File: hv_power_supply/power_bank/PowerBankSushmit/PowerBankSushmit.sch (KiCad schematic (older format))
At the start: 48 parts, among them J1 CONN_01x02, J2 CONN_01x02, J3 USB_A, Q1 SSM3K333R, U1 USB_MicroB, U2 MCP73871T-2CCI_ML-formula, U3 TPS61090RSAR-formula

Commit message: Edited paths and references to match the team
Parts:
- removed C1, C2, C3, C4: C_10uF, footprints:C_0805_OEM, symbol formula:C_10uF-formula
- removed C5: C_10nF, footprints:C_0805_OEM, symbol formula:C_10nF-formula
- removed C6: C_2.2uF, footprints:C_0805_OEM, symbol formula:C_10uF-formula
- removed C7: C_100uF, footprints:C_0805_OEM, symbol formula:C_10uF-formula
- removed D1, D3, D4: LED_0805, footprints:LED_0805_OEM, symbol formula:LED_0805-formula
- removed D2: LED_0805_Amber, footprints:LED_0805_OEM, symbol formula:LED_0805_Amber-formula
- removed F1: 1.5A_Fuse, footprints:Fuse_1206, symbol formula:1.5A_Fuse-formula
- removed J1, J2: CONN_01x02, Connector_PinHeader_2.54mm:PinHeader_1x02_P2.54mm_Vertical, symbol formula:CONN_01x02-formula
- removed L1: L_6.8uH, symbol formula:L_6.8uH-formula
- removed Q1: SSM3K333R, footprints:SOT-23F, symbol formula:SSM3K333R-formula
- removed R1: R_75K, footprints:R_0805_OEM, symbol formula:formula_R_1K
- removed R10, R8: R_100K, footprints:R_0805_OEM, symbol formula:formula_R_1K
- removed R11, R5: R_1.87M, footprints:R_0805_OEM, symbol formula:formula_R_1K
- removed R12, R9: R_200K, footprints:R_0805_OEM, symbol formula:formula_R_1K
- removed R13, R17: R_1k, footprints:R_0805_OEM, symbol formula:formula_R_1K
- removed R14, R16, R18: R_1K, footprints:R_0805_OEM, symbol formula:formula_R_1K
- removed R15: R_10K, footprints:R_0805_OEM, symbol formula:formula_R_1K
- removed R2, R4: R_49.9K, footprints:R_0805_OEM, symbol formula:formula_R_1K
- removed R3: R_43K, footprints:R_0805_OEM, symbol formula:formula_R_1K
- removed R6: R_340K, footprints:R_0805_OEM, symbol formula:formula_R_1K
- removed R7: R_270K, footprints:R_0805_OEM, symbol formula:formula_R_1K
- removed TP1, TP2, TP3, TP4, TP5: TP, footprints:tp_1.6mm, symbol formula:TP-formula
- removed U1: USB_MicroB, Connectors_USB:USB_Micro-B_Molex-105017-0001, symbol formula:USB_MicroB-formula
- removed U2: MCP73871T-2CCI_ML-formula, footprints:MCP73871T, symbol formula:MCP73871T-2CCI_ML-formula
- removed U3: TPS61090RSAR-formula, footprints:TPS61090RSAR, symbol formula:TPS61090RSAR-formula
- added C1, C2, C3, C4: C_10uF, footprints:C_0805_OEM, symbol formula:C_10uF
- added C5: C_10nF, footprints:C_0805_OEM, symbol formula:C_10nF
- added C6: C_2.2uF, footprints:C_0805_OEM, symbol formula:C_2.2uF
- added C7: C_100uF, footprints:C_1812_OEM, symbol formula:C_100uF
- added D1, D3, D4: LED_0805, footprints:LED_0805_OEM, symbol formula:LED_0805
- added D2: LED_0805_Amber, footprints:LED_0805_OEM, symbol formula:LED_0805_Amber
- added F1: 1.5A_Fuse, footprints:Fuse_1206, symbol formula:1.5A_Fuse
- added J1, J2: CONN_01x02, Connector_PinHeader_2.54mm:PinHeader_1x02_P2.54mm_Vertical, symbol formula:CONN_01x02
- added L1: L_6.8uH, symbol formula:L_6.8uH
- added Q1: SSM3K333R, footprints:SOT-23F, symbol formula:SSM3K333R
- added R1: R_75k, footprints:R_0805_OEM, symbol formula:R_75k
- added R10, R8: R_100K, footprints:R_0805_OEM, symbol formula:R_100K
- added R11, R5: R_1.87M, footprints:R_0805_OEM, symbol formula:R_1.87M
- added R12, R9: R_200K, footprints:R_0805_OEM, symbol formula:R_200K
- added R13, R14, R16, R17, R18: R_1K, footprints:R_0805_OEM, symbol formula:R_1K
- added R15: R_10K, footprints:R_0805_OEM, symbol formula:R_10K
- added R2, R4: R_49.9K, footprints:R_0805_OEM, symbol formula:R_49.9K
- added R3: R_43k, footprints:R_0805_OEM, symbol formula:R_43k
- added R6: R_340K, footprints:R_0805_OEM, symbol formula:R_340K
- added R7: R_270K, footprints:R_0805_OEM, symbol formula:R_270K
- added TP1, TP2, TP3, TP4, TP5: TP, footprints:tp_1.6mm, symbol formula:TP
- added U1: USB_MicroB, Connectors_USB:USB_Micro-B_Molex-105017-0001, symbol formula:USB_MicroB
- added U2: MCP73871T-2CCI_ML, footprints:MCP73871T, symbol formula:MCP73871T-2CCI_ML
- added U3: TPS61090RSAR, footprints:TPS61090RSAR, symbol formula:TPS61090RSAR
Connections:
- net labels added: GNDPWR, VBATT
- net labels removed: GNDPWR-formula, VBATT-formula
- wire segments 111 -> 109
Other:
- note added: "Resistor values are specific to IOS"
- note removed: "Resistor valyes are specific to IOS"
- moved on the sheet: J3

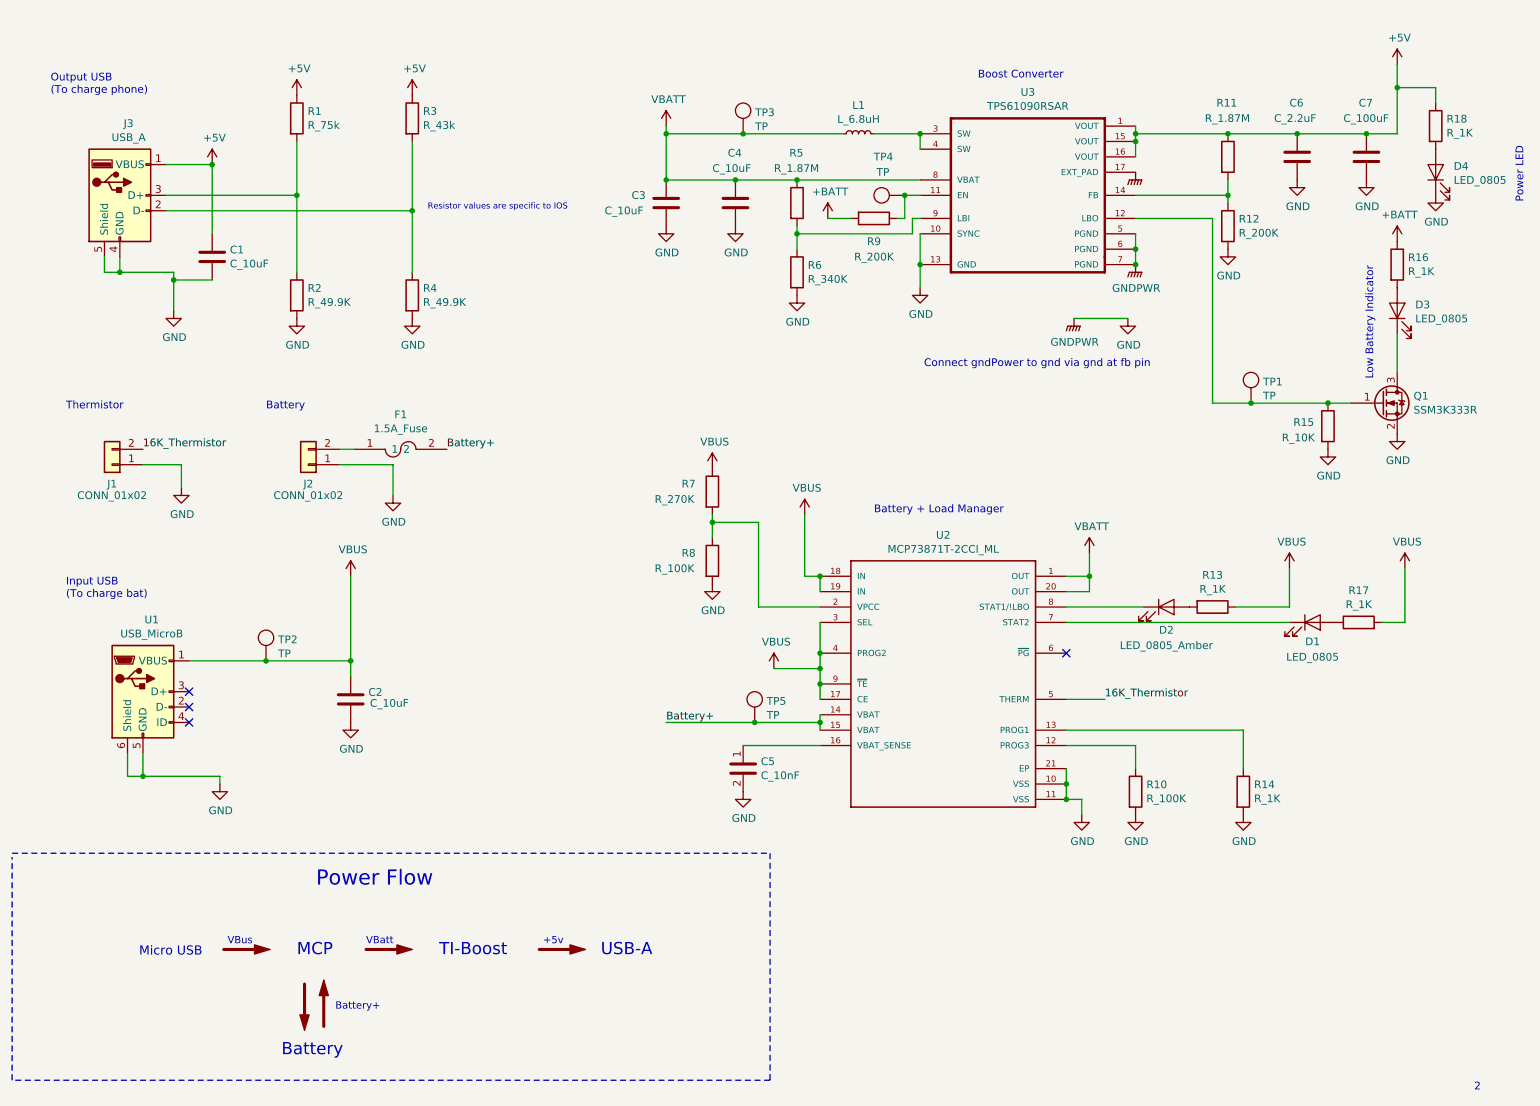
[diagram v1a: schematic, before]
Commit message: Adding draft of PCB Layout and updated schematic
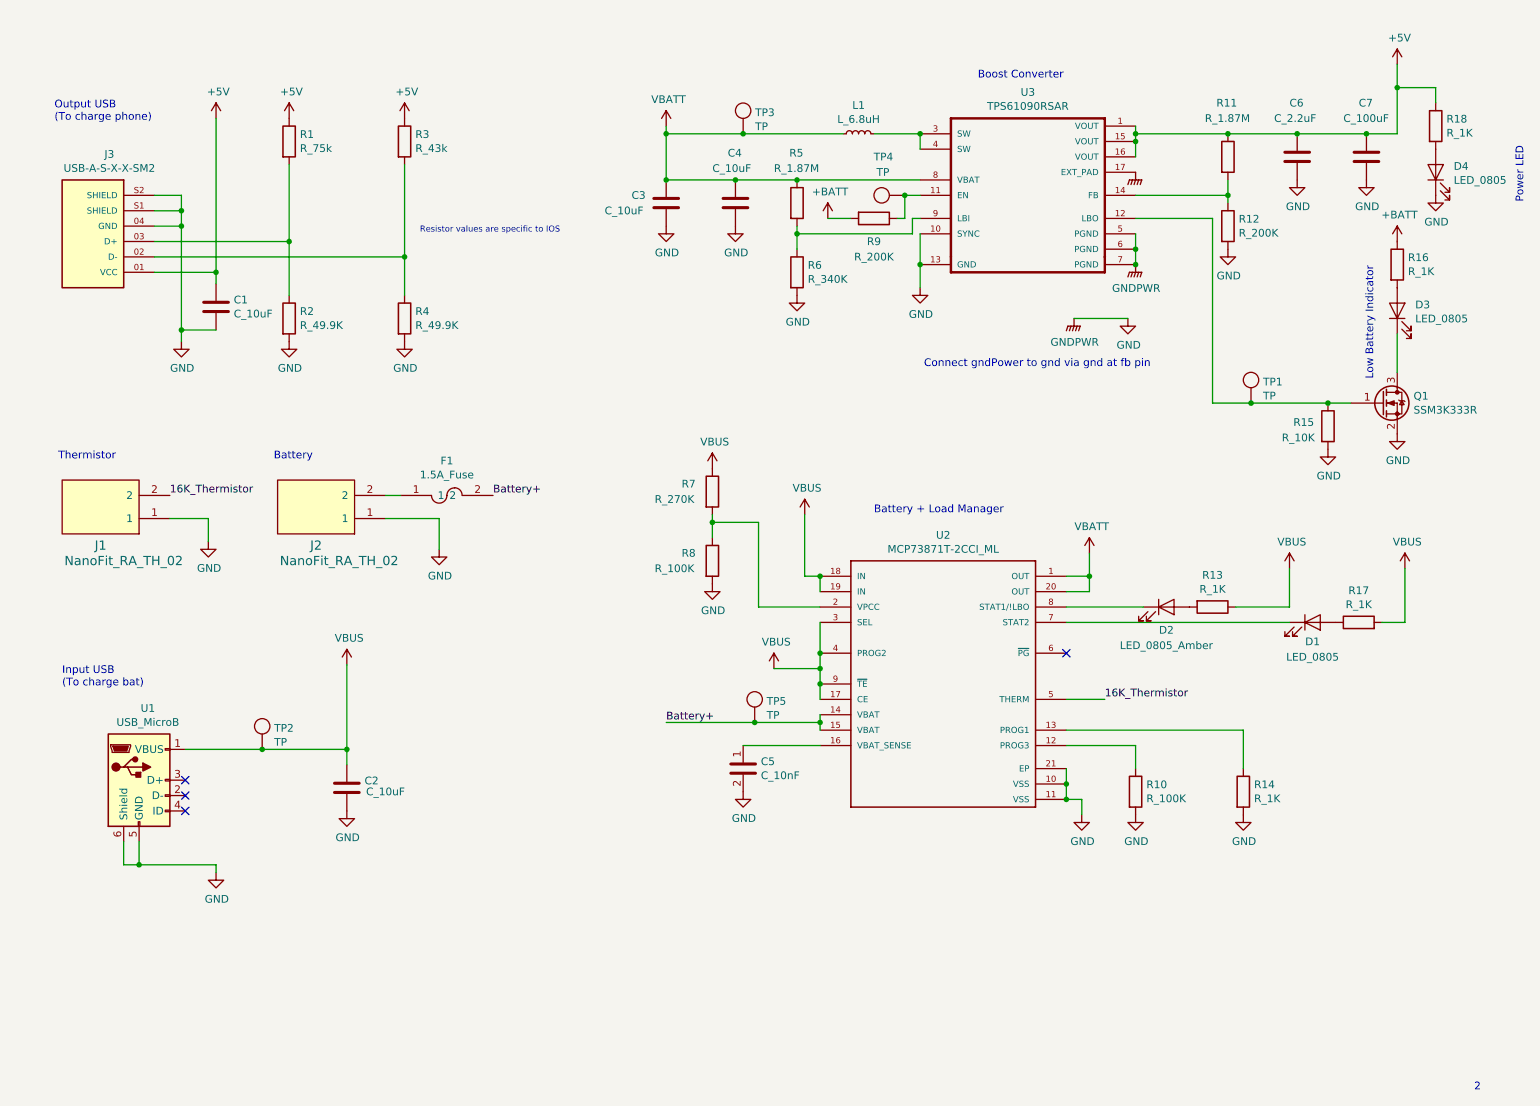
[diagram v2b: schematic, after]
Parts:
- removed Arrow (x5): SYM_Arrow_Large, symbol Graphic:SYM_Arrow_Large
- removed J1, J2: CONN_01x02, Connector_PinHeader_2.54mm:PinHeader_1x02_P2.54mm_Vertical, symbol formula:CONN_01x02
- removed J3: USB_A, symbol Connector:USB_A
- added J1, J2: NanoFit_RA_TH_02, formula:NanoFit_Molex_1x02x2.50mm_Angled_OEM, symbol formula:NanoFit_RA_TH_02
- added J3: USB-A-S-X-X-SM2, formula:SAMTEC_USB-A-S-X-X-SM2, symbol formula:USB-A-S-X-X-SM2
- C1, C2, C3, C4, C5, C6: footprint footprints:C_0805_OEM -> formula:C_0805_OEM
- C7: footprint footprints:C_1812_OEM -> formula:C_1812_4532Metric
- D1, D2, D3, D4: footprint footprints:LED_0805_OEM -> formula:LED_0805_OEM
- F1: footprint footprints:Fuse_1206 -> formula:Fuse_1206
- L1: footprint (none) -> formula:L_100uH_OEM
- Q1: footprint footprints:SOT-23F -> formula:SOT-23F
- R1, R10, R11, R12, R13, R14, R15, R16, R17, R18, R2, R3, R4, R5, R6, R7, R8, R9: footprint footprints:R_0805_OEM -> formula:R_0805_OEM
- TP1, TP2, TP3, TP4, TP5: footprint footprints:tp_1.6mm -> formula:tp_1.6mm
- U1: footprint Connectors_USB:USB_Micro-B_Molex-105017-0001 -> formula:USB_Micro-B
- U2: footprint footprints:MCP73871T -> formula:MCP73871T
- U3: footprint footprints:TPS61090RSAR -> formula:TPS61090RSAR
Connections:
- net +5V: now also J3.01 (VCC)
- net 16K_Thermistor: now also J1.2
- net GND: now also J1.1, J2.1, J3.04 (GND), J3.S1 (SHIELD), J3.S2 (SHIELD)
- net at R3.2, R4.1: now also J3.02 (D-)
- net at R1.2, R2.1: now also J3.03 (D+)
- net at F1.1: now also J2.2
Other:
- note removed: "+5v\n"
- note removed: "Battery+\n"
- note removed: "MCP\n"
- note removed: "Micro USB\n"
- note removed: "Power Flow"
- note removed: "TI-Boost\n"
- note removed: "USB-A\n"
- note removed: "VBatt\n"
- note removed: "VBus"
- moved on the sheet: C2, F1, TP2, U1

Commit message: Updated PCB Layout
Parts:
- removed U1: USB_MicroB, formula:USB_Micro-B, symbol formula:USB_MicroB
- added U1: USB-Micro-1981568-1, formula:TE_1981568-1, symbol formula:USB-Micro-1981568-1
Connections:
- net GND: now also U1.10 (SHIELD), U1.11 (SHIELD), U1.5 (GND), U1.6 (SHIELD), U1.7 (SHIELD), U1.8 (SHIELD), U1.9 (SHIELD)
- net VBUS: now also U1.1 (VCC)
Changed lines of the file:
@@
 L power:GND #PWR0109
 U 1 1 5F906C2E
-P 2425 6225
-F 0 "#PWR0109" H 2425 5975 50  0001 C CNN
-F 1 "GND" H 2430 6052 50  0000 C CNN
-F 2 "" H 2425 6225 50  0001 C CNN
-F 3 "" H 2425 6225 50  0001 C CNN
-	1    2425 6225
+P 2325 6200
+F 0 "#PWR0109" H 2325 5950 50  0001 C CNN
+F 1 "GND" H 2330 6027 50  0000 C CNN
+F 2 "" H 2325 6200 50  0001 C CNN
+F 3 "" H 2325 6200 50  0001 C CNN
+	1    2325 6200
 	1    0    0    -1
 $EndComp
@@
 	3275 4875 3275 5425
 Connection ~ 3275 5425
-Wire Wire Line
-	1825 6025 1825 6175
-Wire Wire Line
-	1825 6175 1925 6175
-Wire Wire Line
-	2425 6175 2425 6225
-Wire Wire Line
-	1925 6025 1925 6175
-Connection ~ 1925 6175
-Wire Wire Line
-	1925 6175 2425 6175
 NoConn ~ 2225 5625
 NoConn ~ 2225 5725
-NoConn ~ 2225 5825
+NoConn ~ 2225 5525
 $Comp
 L power:GND #PWR0111
@@
 	6350 4900 6350 5000
 $Comp
-L formula:USB_MicroB U1
-U 1 1 5FA5499B
-P 1925 5625
-F 0 "U1" H 1982 6092 50  0000 C CNN
-F 1 "USB_MicroB" H 1982 6001 50  0000 C CNN
-F 2 "formula:USB_Micro-B" H 1875 5975 50  0001 C CNN
-F 3 "https://www.molex.com/pdm_docs/sd/1050170001_sd.pdf" H 1875 5975 50  0001 C CNN
-F 4 "DK" H 2175 5375 50  0001 C CNN "MFN"
-F 5 "WM1399CT-ND" H 2275 5475 50  0001 C CNN "MPN"
-F 6 "https://www.digikey.com/product-detail/en/molex-llc/1050170001/WM1399CT-ND/2350885" H 2375 5575 50  0001 C CNN "PurchasingLink"
-	1    1925 5625
-	1    0    0    -1
-$EndComp
-$Comp
 L formula:TP TP2
 U 1 1 5FA633AD
@@
 Wire Wire Line
 	7000 2275 7000 2425
+$Comp
+L formula:USB-Micro-1981568-1 U1
+U 1 1 5FD810EB
+P 1925 5725
+F 0 "U1" H 1982 6292 50  0000 C CNN
+F 1 "USB-Micro-1981568-1" H 1982 6201 50  0000 C CNN
+F 2 "formula:TE_1981568-1" H 1725 6275 50  0001 L BNN
+F 3 "https://www.te.com/commerce/DocumentDelivery/DDEController?Action=srchrtrv&DocNm=1981568&DocType=Customer+Drawing&DocLang=English" H 1925 5725 50  0001 L BNN
+F 4 ".65 mm[.025 in]" H 1875 6275 50  0001 L BNN "Field4"
+F 5 "Connector" H 1325 6075 50  0001 L BNN "Field5"
+F 6 "1981568-1" H 1825 6275 50  0001 L BNN "Field6"
+F 7 "1981568-1" H 2075 6175 50  0001 C CNN "MPN"
+F 8 "https://www.digikey.com/en/products/detail/te-connectivity-amp-connectors/1981568-1/1786248?s=N4IgTCBcDaIIwE4AccCsA2JBaOIC6AvkA" H 1725 6275 50  0001 C CNN "Purchasing Link"
+	1    1925 5725
+	1    0    0    -1
+$EndComp
+Wire Wire Line
+	2225 5825 2325 5825
+Wire Wire Line
+	2325 5825 2325 6025
+Wire Wire Line
+	2225 6025 2325 6025
+Connection ~ 2325 6025
+Wire Wire Line
+	2325 6025 2325 6200
 $EndSCHEMATC
